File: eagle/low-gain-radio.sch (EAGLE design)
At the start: 108 parts, among them Y1 32MHz

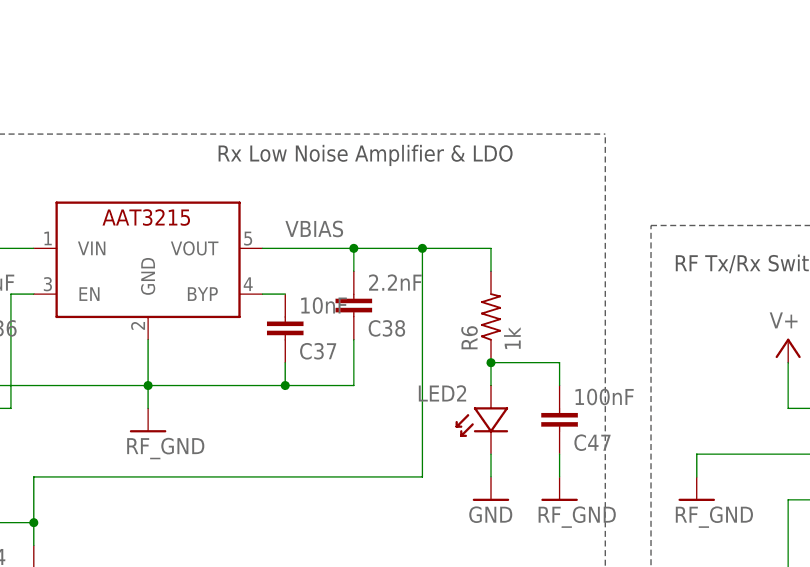
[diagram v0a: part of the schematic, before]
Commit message: Updated passive components with attributes for BOM
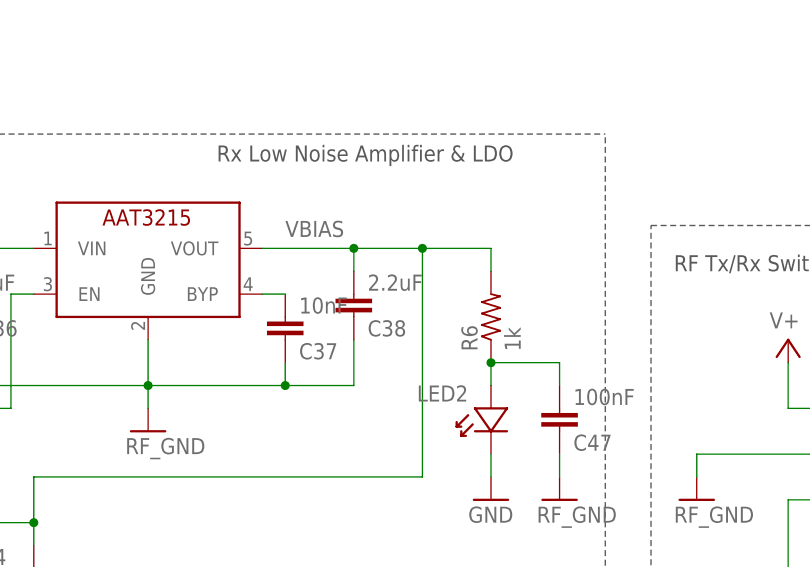
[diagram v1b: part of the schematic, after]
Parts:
- C1, C16, C18, C20, C21, C3, C37, C40: DIST (none) -> Digi-Key; DPN (none) -> 490-1512-2-ND; MFG (none) -> Murata; MFG_PN (none) -> GRM188R71H103KA01D
- C10, C5, C6, C9: DIST (none) -> Digi-Key; DPN (none) -> 490-1407-2-ND; MFG (none) -> Murata; MFG_PN (none) -> GRM1885C1H150JA01D
- C11, C12: DIST (none) -> Digi-Key; DPN (none) -> 06031U8R2BAT2A-ND; MFG (none) -> AVX; MFG_PN (none) -> 06031U8R2BAT2A
- C13, C15, C17, C19, C22, C46: DIST (none) -> Digi-Key; DPN (none) -> 490-6405-2-ND; MFG (none) -> Murata; MFG_PN (none) -> GRM188R60J106ME47J
- C14, C26, C27, C28, C29, C30, C31, C32, C33, C42, C45, C47, C48: DIST (none) -> Digi-Key; DPN (none) -> 478-5778-1-ND; MFG (none) -> AVX; MFG_PN (none) -> 06035C104JAT2A
- C2, C4: DIST (none) -> Digi-Key; DPN (none) -> 490-1405-2-ND; MFG (none) -> Murata; MFG_PN (none) -> GRM1885C1H120JA01D
- C23, C24, C25: DIST (none) -> Digi-key; DPN (none) -> 490-1303-1-ND; MFG (none) -> Murata; MFG_PN (none) -> GRM155R71H102KA01D
- C34, C35: DIST (none) -> Digi-Key; DPN (none) -> GQM1875C2E6R0BB12D-ND; MFG (none) -> Murata; MFG_PN (none) -> GQM1875C2E6R0BB12D
- C36, C39: DIST (none) -> Digi-Key; DPN (none) -> 490-1543-2-ND; MFG (none) -> Murata; MFG_PN (none) -> GRM188R61A105KA61D
- C38: value 2.2nF -> 2.2uF; DIST (none) -> Digi-Key; DPN (none) -> 478-3492-2-ND; MFG (none) -> AVX; MFG_PN (none) -> SQCSVA2R2BAT1A
- C41: DIST (none) -> Digi-Key; DPN (none) -> 478-3492-2-ND; MFG (none) -> AVX; MFG_PN (none) -> SQCSVA2R2BAT1A
- C43: DIST (none) -> Digi-Key; DPN (none) -> 478-1704-1-ND; MFG (none) -> AVX; MFG_PN (none) -> TAJC107K010RNJ
- C44: DIST (none) -> Digi-key; DPN (none) -> 490-4516-1-ND; MFG (none) -> Murata; MFG_PN (none) -> GRM155R71H103KA88D
- C7, C8: DIST (none) -> Digi-Key; DPN (none) -> 490-9668-2-ND; MFG (none) -> Murata; MFG_PN (none) -> GRM1885C1H2R2CA01D
- L1, L2: DIST (none) -> Digi-Key; DPN (none) -> 490-6874-1-ND; MFG (none) -> Murata; MFG_PN (none) -> LQW18AN22NG00D
- L3, L4, L5, L6: DIST (none) -> Digi-Key; DPN (none) -> 490-6866-1-ND; MFG (none) -> Murata; MFG_PN (none) -> LQW18AN15NG00D
- L8: DIST (none) -> Digi-Key; DPN (none) -> 490-6912-2-ND; MFG (none) -> Murata; MFG_PN (none) -> LQW18AN82NG00D
- R1: DIST (none) -> Digi-Key; DPN (none) -> 1276-4592-2-ND; MFG (none) -> Samsung; MFG_PN (none) -> RC1608F2490CS
- R10, R11, R12, R4, R6, R7, R8, R9: DIST (none) -> Digi-Key; DPN (none) -> 311-1.00KHRCT-ND; MFG (none) -> Yageo; MFG_PN (none) -> RC0603FR-071KL
- R2, R3, R5: DIST (none) -> Digi-Key; DPN (none) -> 311-10.0KHRCT-ND; MFG (none) -> Yageo; MFG_PN (none) -> RC0603FR-0710KL

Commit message: Added test point names, fixed some ugly traces
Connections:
- net N$11 renamed V_SPI
- net N$12 renamed LDO_EN
- net N$3 renamed DIO2
- net N$5 renamed DIO3
- net N$6 renamed XTA
- net N$9 renamed DIO4
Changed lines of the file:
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@@
 <attribute name="MFN-PN" x="381" y="198.12" size="1.778" layer="96" display="off"/>
 </instance>
-<instance part="U$1" gate="G$1" x="116.84" y="312.42" rot="MR0"/>
+<instance part="U$1" gate="G$1" x="109.22" y="302.26" rot="MR0"/>
 <instance part="U$2" gate="G$1" x="378.46" y="129.54"/>
 <instance part="U$3" gate="G$1" x="299.72" y="175.26"/>
@@
 </segment>
 </net>
-<net name="N$6" class="0">
+<net name="XTA" class="0">
 <segment>
 <pinref part="KW0X" gate="G$1" pin="XTA"/>
@@
 </segment>
 </net>
-<net name="N$3" class="0">
+<net name="DIO2" class="0">
 <segment>
 <pinref part="KW0X" gate="G$1" pin="DIO2"/>
@@
 </segment>
 </net>
-<net name="N$5" class="0">
+<net name="DIO3" class="0">
 <segment>
 <pinref part="KW0X" gate="G$1" pin="DIO3"/>
@@
 </segment>
 </net>
-<net name="N$9" class="0">
+<net name="DIO4" class="0">
 <segment>
 <pinref part="KW0X" gate="G$1" pin="DIO4"/>
@@
 </segment>
 </net>
-<net name="N$11" class="0">
+<net name="V_SPI" class="0">
 <segment>
 <wire x1="121.92" y1="287.02" x2="121.92" y2="299.72" width="0.1524" layer="91"/>
@@
 </segment>
 </net>
-<net name="N$12" class="0">
+<net name="LDO_EN" class="0">
 <segment>
 <pinref part="U$8" gate="G$1" pin="EN"/>

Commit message: Added to-do lists
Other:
- note added: "TODO: -Add attributes for rest of parts"
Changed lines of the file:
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@@
 <text x="424.18" y="101.6" size="1.778" layer="97">Inverter prevents RF
 line crossing on layout</text>
+<text x="309.88" y="60.96" size="1.778" layer="100">TODO:
+-Add attributes for rest of parts</text>
 </plain>
 <instances>

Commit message: Pushing for Andrew
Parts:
- CF2: value CON-MCX-LINX -> CON-MCX-F-LINX-CONMCX003.062; device oresat-eagle:CON-MCX-LINX -> oresat-eagle:CON-MCX-F-LINX-CONMCX003.062
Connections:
- removed net ASD: C47.1
- net RF_GND: now also C47.1, CF2.SHIELD
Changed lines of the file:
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@@
 <part name="GND14" library="psas_c3_team05" deviceset="GND" device=""/>
 <part name="CF1" library="oresat-eagle" deviceset="ORESAT-CONNECTOR-40PIN" device=""/>
-<part name="CF2" library="oresat-eagle" deviceset="CON-MCX-LINX" device=""/>
+<part name="CF2" library="oresat-eagle" deviceset="CON-MCX-F-LINX-CONMCX003.062" device=""/>
 <part name="TP18" library="testpad" deviceset="TPS" device="PAD1-13"/>
 <part name="SH1" library="hw-laird-bmi-s-202" deviceset="BMI-S-202-SHIELD" device=""/>
@@
 </segment>
 </net>
-<net name="ASD" class="0">
-<segment>
-<pinref part="C47" gate="CE" pin="1"/>
-<wire x1="426.72" y1="175.26" x2="426.72" y2="172.72" width="0.1524" layer="91"/>
-<pinref part="U$38" gate="G$1" pin="GND"/>
-</segment>
-</net>
 <net name="N$2" class="0">
 <segment>
@@
 <wire x1="502.92" y1="167.64" x2="510.54" y2="167.64" width="0.1524" layer="91"/>
 <wire x1="510.54" y1="167.64" x2="510.54" y2="165.1" width="0.1524" layer="91"/>
+<pinref part="CF2" gate="G$1" pin="SHIELD"/>
+<wire x1="510.54" y1="170.18" x2="510.54" y2="167.64" width="0.1524" layer="91"/>
+<junction x="510.54" y="167.64"/>
 </segment>
 <segment>
@@
 <junction x="144.78" y="210.82"/>
 </segment>
-</net>
+<segment>
+<pinref part="C47" gate="CE" pin="1"/>
+<wire x1="426.72" y1="175.26" x2="426.72" y2="172.72" width="0.1524" layer="91"/>
+<pinref part="U$38" gate="G$1" pin="GND"/>
+</segment>
+</net>

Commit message: Fixed RF_GND/GND warnings by creating new RF_GND symbol in oresat-eagle-libraries. Added bypass cap on TX/RX inverter.
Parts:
- added C49: 100nF, rcl_custom:C-EU0603-B-NOSILK
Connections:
- net GND: no longer C36.1, C37.1, C38.1, C48.1, U$7.GND
- net RF_GND: now also C36.1, C37.1, C38.1, C48.1, C49.1, U$7.GND
- net V+: now also C49.2
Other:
- note added: "= 3.0V"
- moved on the sheet: U$39G$2

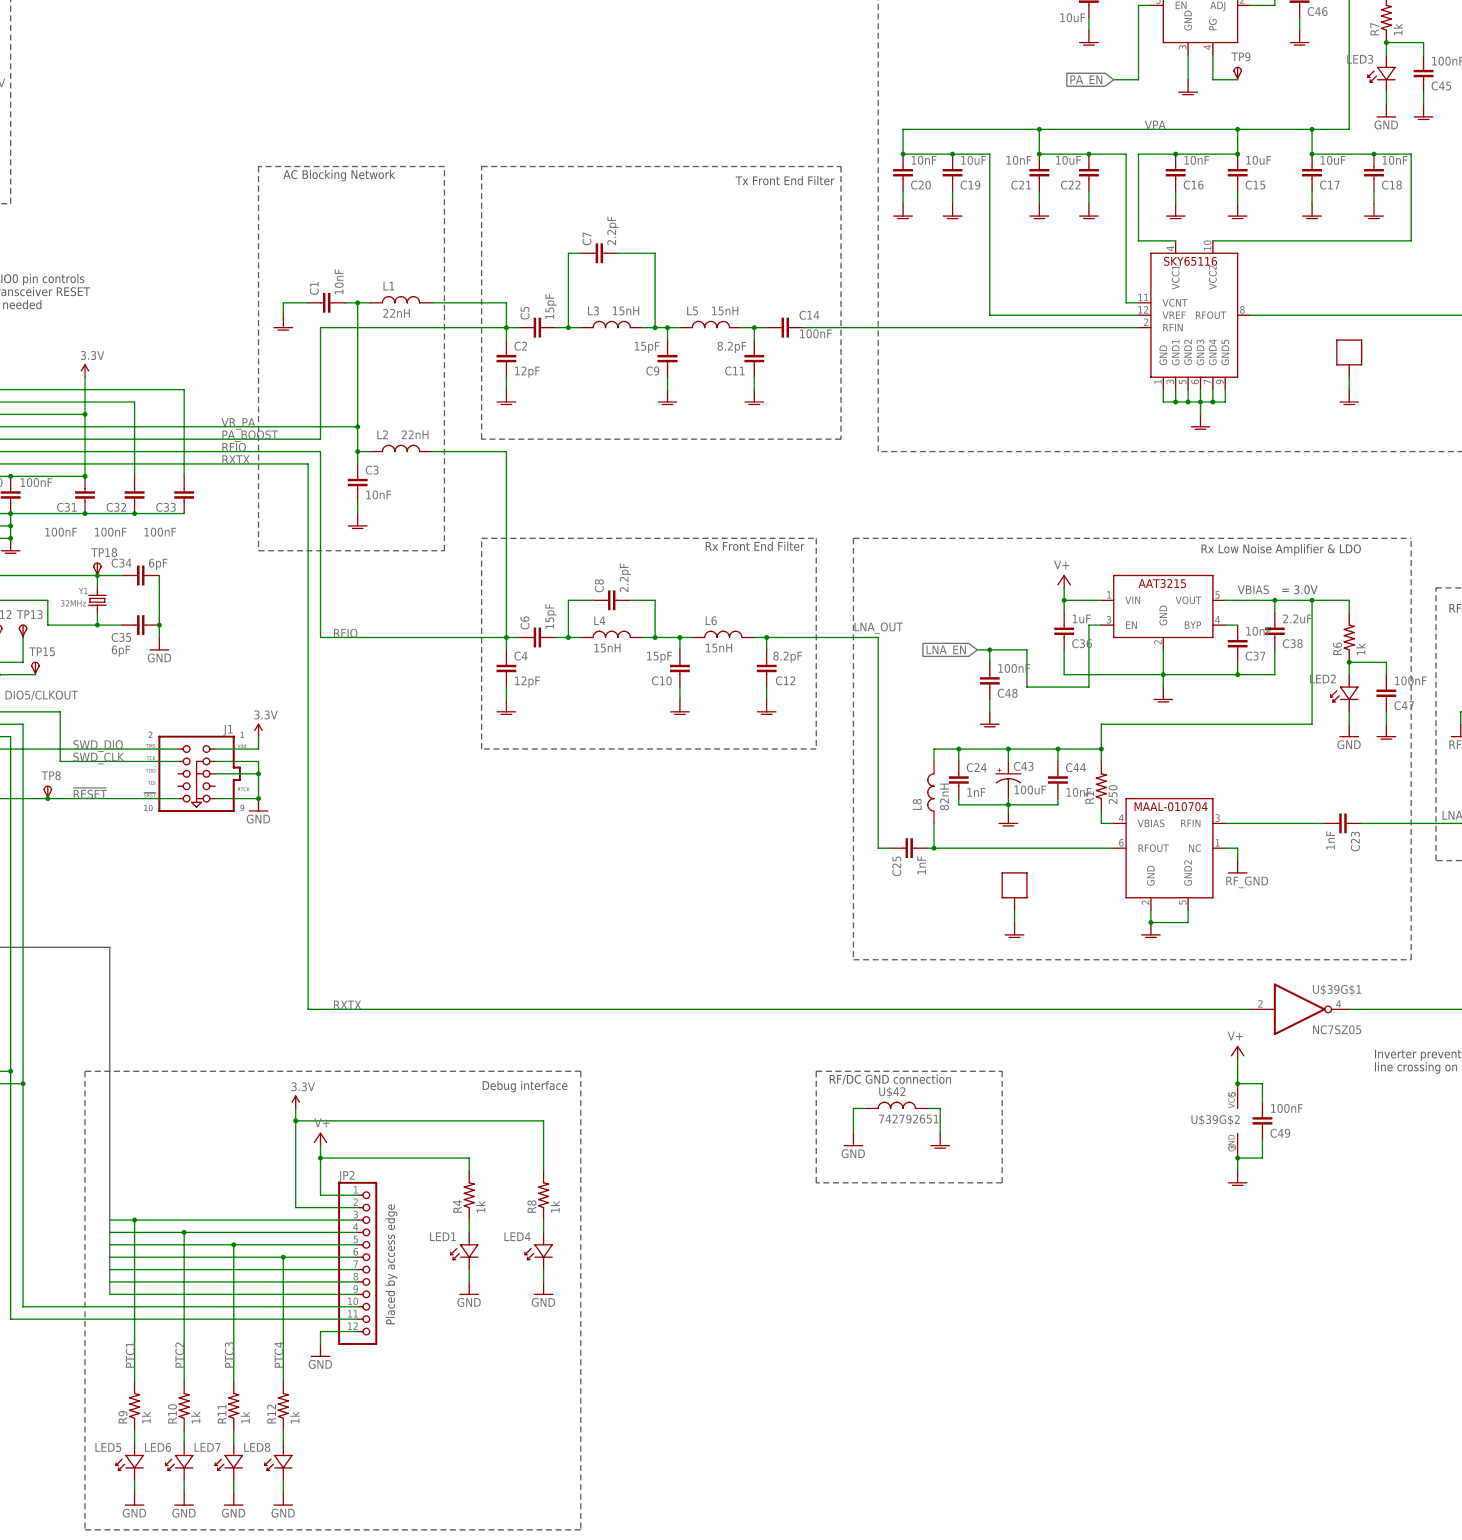
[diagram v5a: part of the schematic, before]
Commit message: Updated all attributes for forming BOM
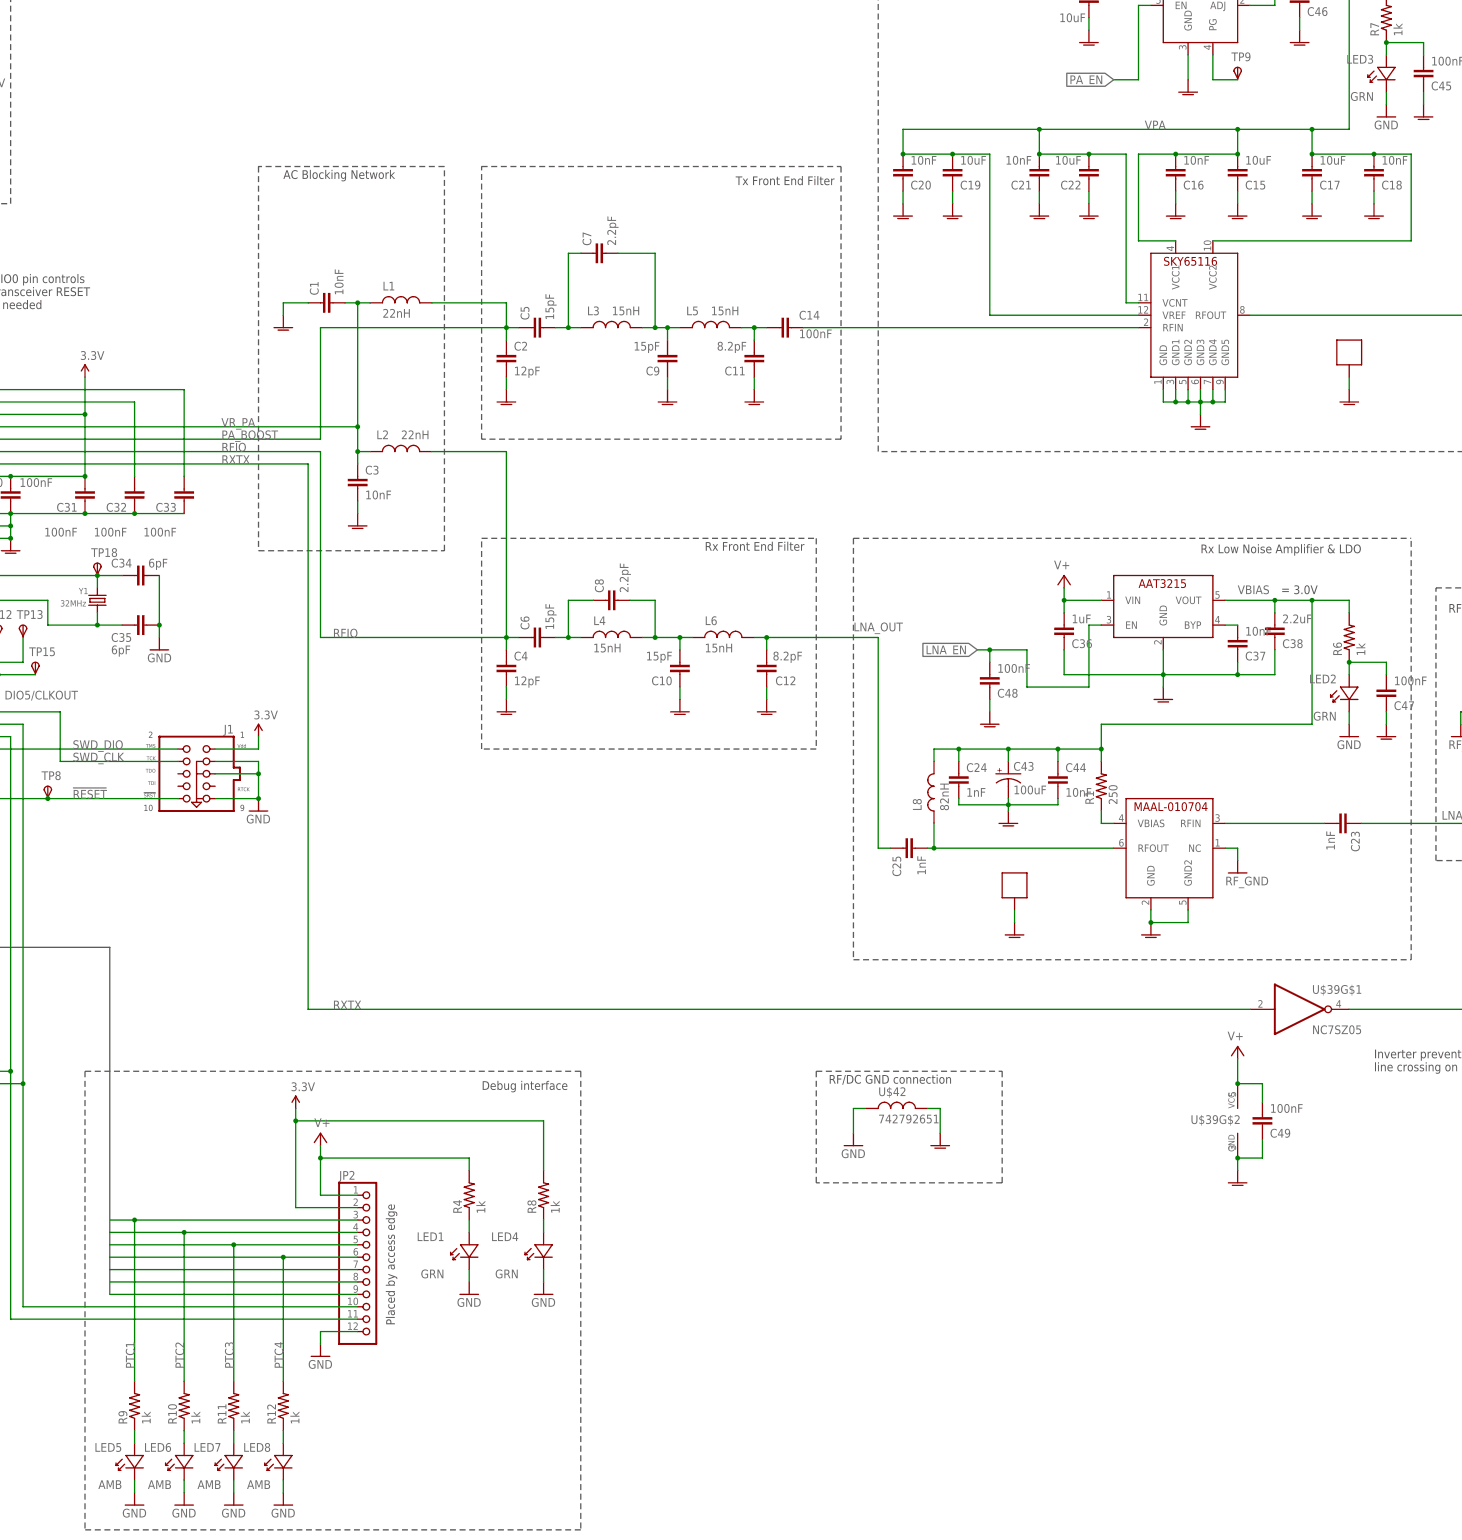
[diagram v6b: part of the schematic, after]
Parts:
- LED1, LED2, LED3, LED4: value (none) -> GRN; DIST (none) -> Digi-Key; DPN (none) -> 160-1446-1-ND; MFG (none) -> Lite-On Inc.; MFG_PN (none) -> LTST-C191KGKT
- LED5, LED6, LED7, LED8: value (none) -> AMB; DIST (none) -> Digi-Key; DPN (none) -> 160-1440-1-ND; MFG (none) -> Lite-On Inc.; MFG_PN (none) -> LTST-C191AKT
- PA: DIST (none) -> Skyworks; DPN (none) -> SKY65116
- TRSWITCH: DIST (none) -> Digi-Key; DPN (none) -> 863-1649-1-ND
- U$1: DIST (none) -> Digi-Key; DPN (none) -> W25Q80DVSSIG-ND; MFG (none) -> Winbond Electronics; MFG_PN (none) -> W25Q80DVSSIG
- U$39: DIST (none) -> Digi-Key; DPN (none) -> NC7SZ05P5XTR-ND; MFG (none) -> Fairchild Semiconductor; MFG_PN (none) -> NC7SZ05P5X
- U$42: DIST (none) -> Digi-Key; DPN (none) -> 732-1593-2-ND; MFG (none) -> Wurth Electronics Inc; MFG_PN (none) -> 742792651
- U$7, U$8: DIST (none) -> Skyworks; DPN (none) -> AAT3215
- U$9: DIST (none) -> Digi-Key; DPN (none) -> 497-15229-2-ND; MFG (none) -> STMicroelectronics; MFG_PN (none) -> LD39200PU33R

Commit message: Minor board adjustments
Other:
- note removed: "TODO: -Add attributes for rest of parts"
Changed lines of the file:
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@@
 <text x="424.18" y="101.6" size="1.778" layer="97">Inverter prevents RF
 line crossing on layout</text>
-<text x="309.88" y="60.96" size="1.778" layer="100">TODO:
--Add attributes for rest of parts</text>
 <text x="405.13" y="199.39" size="1.778" layer="97">= 3.0V</text>
 <text x="410.21" y="326.39" size="1.778" layer="97">= 3.0V</text>
